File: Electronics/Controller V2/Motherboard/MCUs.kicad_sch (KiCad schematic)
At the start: 18 parts, among them J5 Pulse_J0011D01BNL, J7 Pulse_J0011D01BNL

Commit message: Working on V2 controller PCB.
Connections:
- net CAN_RX: no longer U5.45 (GPIO23_CRX1)
- net CAN_TX: no longer U5.44 (GPIO22_CTX1)
- no-connect marks 47 -> 49
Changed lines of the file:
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@@
   (no_connect (at 174.625 52.07))
   (no_connect (at 63.5 95.25))
+  (no_connect (at 235.585 46.99))
   (no_connect (at 174.625 95.25))
   (no_connect (at 174.625 97.79))
@@
   (no_connect (at 174.625 92.71))
   (no_connect (at 235.585 82.55))
+  (no_connect (at 235.585 49.53))
   (no_connect (at 174.625 49.53))
   (no_connect (at 235.585 59.69))
@@
     (stroke (width 0) (type default))
   )
-  (wire (pts (xy 235.585 46.99) (xy 247.015 46.99))
-    (stroke (width 0) (type default))
-  )
   (wire (pts (xy 92.71 116.84) (xy 90.17 116.84))
     (stroke (width 0) (type default))
@@
     (stroke (width 0) (type default))
   )
-  (wire (pts (xy 235.585 49.53) (xy 247.015 49.53))
-    (stroke (width 0) (type default))
-  )
   (wire (pts (xy 59.055 92.71) (xy 63.5 92.71))
     (stroke (width 0) (type default))
@@
     (stroke (width 0) (type default))
   )
-  (label "CAN_RX" (at 130.81 46.99 0) (fields_autoplaced)
-    (effects (font (size 1.27 1.27)) (justify left bottom))
-  )
-  (label "CAN_TX" (at 130.81 49.53 0) (fields_autoplaced)
-    (effects (font (size 1.27 1.27)) (justify left bottom))
-  )
   (hierarchical_label "IMU_SCK" (shape output) (at 133.985 72.39 0) (fields_autoplaced)
     (effects (font (size 1.27 1.27)) (justify left))
@@
     (effects (font (size 1.27 1.27)) (justify right))
   )
-  (hierarchical_label "CAN_TX" (shape output) (at 247.015 49.53 0) (fields_autoplaced)
+  (hierarchical_label "CAN_TX" (shape output) (at 130.81 49.53 0) (fields_autoplaced)
     (effects (font (size 1.27 1.27)) (justify left))
   )
@@
     (effects (font (size 1.27 1.27)) (justify left))
   )
-  (hierarchical_label "CAN_RX" (shape input) (at 247.015 46.99 0) (fields_autoplaced)
-    (effects (font (size 1.27 1.27)) (justify left))
-  )
+  (hierarchical_label "CAN_RX" (shape input) (at 130.81 46.99 0) (fields_autoplaced)
+    (effects (font (size 1.27 1.27)) (justify left))
+  )

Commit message: Added missing ground connection. Working on PCB layout.
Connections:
- net GPIO_G1: now also U4.38 (GPIO16_RX4_SCL1); no longer U4.41 (GPIO19_SCL0)
- net GPIO_G2: now also U4.39 (GPIO17_TX4_SDA1); no longer U4.40 (GPIO18_SDA0)
- net GPIO_G3: now also U4.40 (GPIO18_SDA0); no longer U4.39 (GPIO17_TX4_SDA1)
- net GPIO_G4: now also U4.41 (GPIO19_SCL0); no longer U4.38 (GPIO16_RX4_SCL1)
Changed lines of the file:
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@@
   (title_block
     (title "Tandem Leveller Controller")
-    (date "2026-02-02")
+    (date "2026-02-06")
     (rev "V2.0")
     (company "(C) andy@britishideas.com 2026")
@@
     (effects (font (size 1.27 1.27)) (justify right))
   )
-  (hierarchical_label "GPIO_G2" (shape bidirectional) (at 133.985 59.69 0) (fields_autoplaced)
+  (hierarchical_label "GPIO_G2" (shape bidirectional) (at 133.985 62.23 0) (fields_autoplaced)
     (effects (font (size 1.27 1.27)) (justify left))
   )
@@
     (effects (font (size 1.27 1.27)) (justify left))
   )
-  (hierarchical_label "GPIO_G4" (shape bidirectional) (at 133.985 64.77 0) (fields_autoplaced)
+  (hierarchical_label "GPIO_G4" (shape bidirectional) (at 133.985 57.15 0) (fields_autoplaced)
     (effects (font (size 1.27 1.27)) (justify left))
   )
@@
     (effects (font (size 1.27 1.27)) (justify right))
   )
-  (hierarchical_label "GPIO_G3" (shape bidirectional) (at 133.985 62.23 0) (fields_autoplaced)
+  (hierarchical_label "GPIO_G3" (shape bidirectional) (at 133.985 59.69 0) (fields_autoplaced)
     (effects (font (size 1.27 1.27)) (justify left))
   )
@@
     (effects (font (size 1.27 1.27)) (justify left))
   )
-  (hierarchical_label "GPIO_G1" (shape bidirectional) (at 133.985 57.15 0) (fields_autoplaced)
-    (effects (font (size 1.27 1.27)) (justify left))
-  )
+  (hierarchical_label "GPIO_G1" (shape bidirectional) (at 133.985 64.77 0) (fields_autoplaced)
+    (effects (font (size 1.27 1.27)) (justify left))
+  )

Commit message: Added generic IMU option.
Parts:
- added J10: ORIENT, Connector_PinHeader_2.54mm:PinHeader_1x02_P2.54mm_Vertical, symbol Connector_Generic:Conn_01x02
- added J11: OPT, Connector_PinHeader_2.54mm:PinHeader_1x02_P2.54mm_Vertical, symbol Connector_Generic:Conn_01x02
- added R22, R23: 10k, Resistor_SMD:R_0805_2012Metric, symbol Device:R
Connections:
- net +5V: now also R22.2, R23.2
- net GND: now also J10.1 (Pin_1), J11.1 (Pin_1)
- net at U4.18 (GPIO26_MOSI1): now also J10.2 (Pin_2), R22.1
- net at U4.19 (GPIO27_SCK1): now also J11.2 (Pin_2), R23.1
- net GPIO_G1 renamed GPIO_G1_RX
- net GPIO_G2 renamed GPIO_G2_TX
- no-connect marks 49 -> 47
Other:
- moved on the sheet: R1, R2

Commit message: Added relay to control output of valve E.
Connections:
- net VALVE_E_EN: now reaches U4.25 (GPIO33)
- no-connect marks 47 -> 46
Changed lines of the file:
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@@
   (title_block
     (title "Tandem Leveller Controller")
-    (date "2026-02-09")
+    (date "2026-03-01")
     (rev "V2.0")
     (company "(C) andy@britishideas.com 2026")
@@
   (no_connect (at 235.585 85.09))
   (no_connect (at 63.5 100.33))
-  (no_connect (at 124.46 95.25))
   (no_connect (at 63.5 97.79))
   (no_connect (at 235.585 90.17))
@@
     (stroke (width 0) (type default))
   )
+  (wire (pts (xy 124.46 95.25) (xy 133.985 95.25))
+    (stroke (width 0) (type default))
+  )
   (wire (pts (xy 34.925 127) (xy 34.925 139.7))
     (stroke (width 0) (type default))
@@
     (effects (font (size 1.27 1.27)) (justify right))
   )
+  (hierarchical_label "VALVE_E_EN" (shape output) (at 133.985 95.25 0) (fields_autoplaced)
+    (effects (font (size 1.27 1.27)) (justify left))
+  )
   (hierarchical_label "VALVE_E_PWM" (shape output) (at 57.785 67.31 180) (fields_autoplaced)

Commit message: Working on autosteer support for V2 controller.
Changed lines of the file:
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@@
   (title_block
     (title "Tandem Leveller Controller")
-    (date "2026-03-01")
+    (date "2026-03-02")
     (rev "V2.0")
     (company "(C) andy@britishideas.com 2026")
@@
     (effects (font (size 1.27 1.27)) (justify right))
   )
+  (hierarchical_label "WAS_SCL" (shape bidirectional) (at 114.935 168.91 0) (fields_autoplaced)
+    (effects (font (size 1.27 1.27)) (justify left))
+  )
+  (hierarchical_label "WAS_SDA" (shape bidirectional) (at 114.935 166.37 0) (fields_autoplaced)
+    (effects (font (size 1.27 1.27)) (justify left))
+  )
   (symbol (lib_id "power:+5V") (at 93.98 38.1 0) (unit 1)

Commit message: Added WAS circuit.
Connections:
- net GPIO_G3: now also U4.23 (GPIO31_CTX3); no longer U4.40 (GPIO18_SDA0)
- net GPIO_G4: now also U4.24 (GPIO32); no longer U4.41 (GPIO19_SCL0)
- net WAS_SCL: now also U4.41 (GPIO19_SCL0)
- net WAS_SDA: now also U4.40 (GPIO18_SDA0)
- net GPIO_C4: no longer names the net of U4.28 (GPIO36_CS)
- no-connect marks 46 -> 45
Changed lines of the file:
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@@
   (no_connect (at 174.625 59.69))
   (no_connect (at 235.585 95.25))
+  (no_connect (at 124.46 87.63))
   (no_connect (at 63.5 77.47))
   (no_connect (at 235.585 85.09))
-  (no_connect (at 63.5 100.33))
-  (no_connect (at 63.5 97.79))
   (no_connect (at 235.585 90.17))
   (no_connect (at 174.625 72.39))
@@
     (stroke (width 0) (type default))
   )
+  (wire (pts (xy 63.5 97.79) (xy 61.595 97.79))
+    (stroke (width 0) (type default))
+  )
   (wire (pts (xy 205.105 38.1) (xy 205.105 39.37))
     (stroke (width 0) (type default))
@@
     (stroke (width 0) (type default))
   )
+  (wire (pts (xy 61.595 121.285) (xy 66.675 121.285))
+    (stroke (width 0) (type default))
+  )
   (wire (pts (xy 124.46 74.93) (xy 133.985 74.93))
     (stroke (width 0) (type default))
@@
     (stroke (width 0) (type default))
   )
+  (wire (pts (xy 63.5 118.745) (xy 66.675 118.745))
+    (stroke (width 0) (type default))
+  )
   (wire (pts (xy 124.46 95.25) (xy 133.985 95.25))
     (stroke (width 0) (type default))
@@
     (stroke (width 0) (type default))
   )
+  (wire (pts (xy 61.595 97.79) (xy 61.595 121.285))
+    (stroke (width 0) (type default))
+  )
   (wire (pts (xy 271.145 113.665) (xy 271.145 104.775))
     (stroke (width 0) (type default))
@@
     (stroke (width 0) (type default))
   )
-  (wire (pts (xy 124.46 87.63) (xy 133.985 87.63))
-    (stroke (width 0) (type default))
-  )
   (wire (pts (xy 154.94 54.61) (xy 154.94 44.45))
     (stroke (width 0) (type default))
@@
     (stroke (width 0) (type default))
   )
+  (wire (pts (xy 63.5 100.33) (xy 63.5 118.745))
+    (stroke (width 0) (type default))
+  )
   (wire (pts (xy 201.295 116.84) (xy 201.295 118.11))
     (stroke (width 0) (type default))
@@
     (effects (font (size 1.27 1.27)) (justify left))
   )
-  (hierarchical_label "GPIO_G4" (shape bidirectional) (at 133.985 57.15 0) (fields_autoplaced)
-    (effects (font (size 1.27 1.27)) (justify left))
-  )
-  (hierarchical_label "GPIO_C4" (shape bidirectional) (at 133.985 87.63 0) (fields_autoplaced)
+  (hierarchical_label "GPIO_G4" (shape bidirectional) (at 66.675 118.745 0) (fields_autoplaced)
     (effects (font (size 1.27 1.27)) (justify left))
   )
@@
     (effects (font (size 1.27 1.27)) (justify right))
   )
-  (hierarchical_label "GPIO_G3" (shape bidirectional) (at 133.985 59.69 0) (fields_autoplaced)
+  (hierarchical_label "GPIO_G3" (shape bidirectional) (at 66.675 121.285 0) (fields_autoplaced)
     (effects (font (size 1.27 1.27)) (justify left))
   )
@@
     (effects (font (size 1.27 1.27)) (justify right))
   )
-  (hierarchical_label "WAS_SCL" (shape bidirectional) (at 114.935 168.91 0) (fields_autoplaced)
-    (effects (font (size 1.27 1.27)) (justify left))
-  )
-  (hierarchical_label "WAS_SDA" (shape bidirectional) (at 114.935 166.37 0) (fields_autoplaced)
-    (effects (font (size 1.27 1.27)) (justify left))
-  )
+  (hierarchical_label "WAS_SCL" (shape bidirectional) (at 133.985 57.15 0) (fields_autoplaced)
+    (effects (font (size 1.27 1.27)) (justify left))
+  )
+  (hierarchical_label "WAS_SDA" (shape bidirectional) (at 133.985 59.69 0) (fields_autoplaced)
+    (effects (font (size 1.27 1.27)) (justify left))
+  )

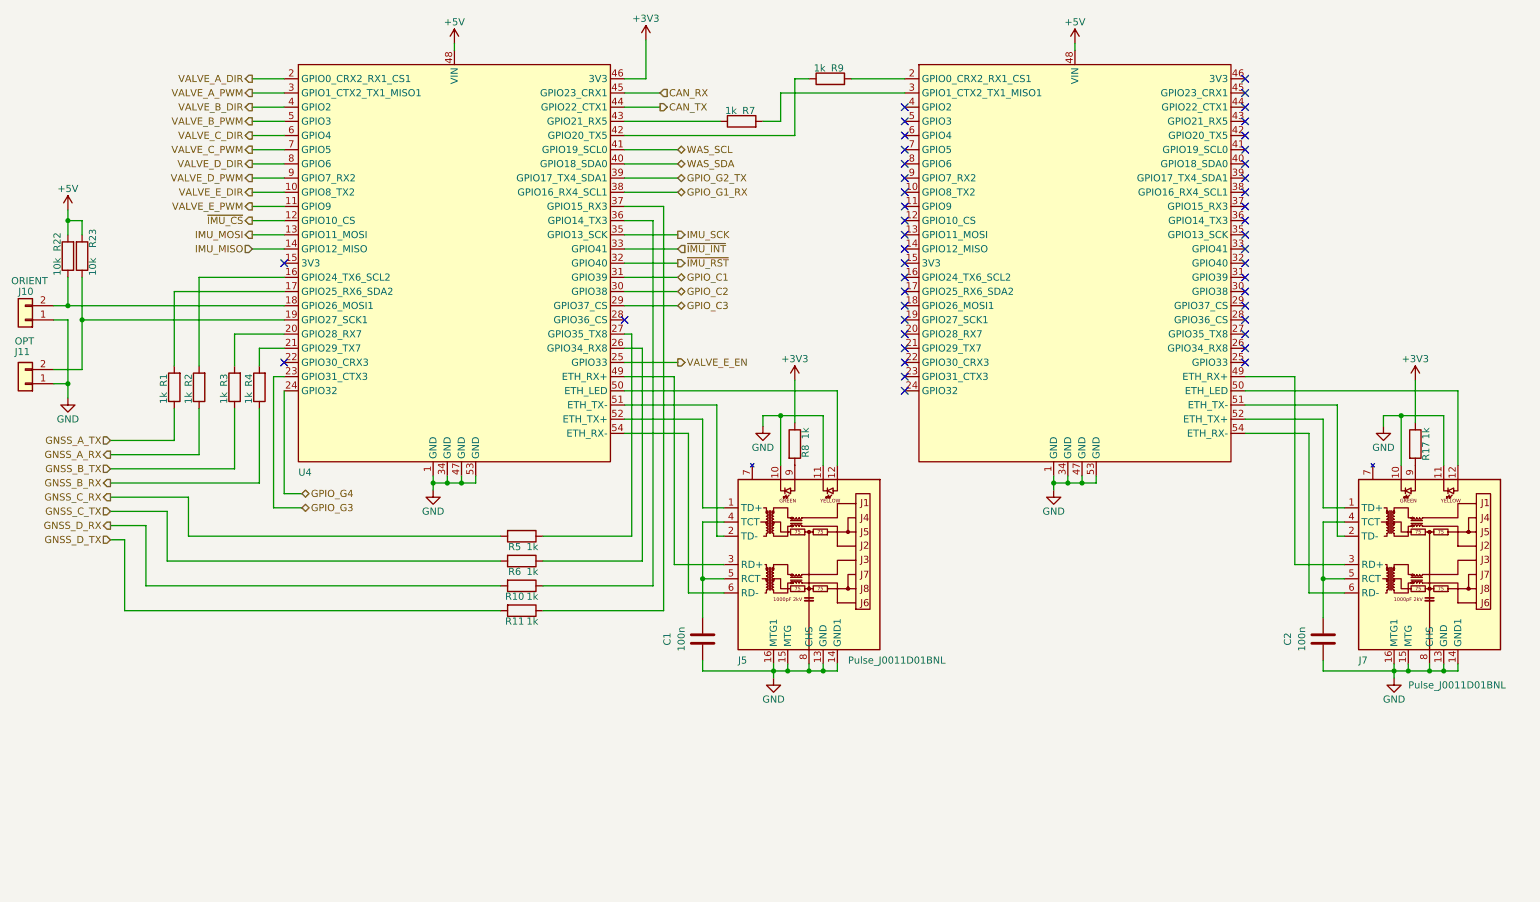
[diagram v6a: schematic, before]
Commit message: Added connector and mounting holes for future USB-C PD expansion board.
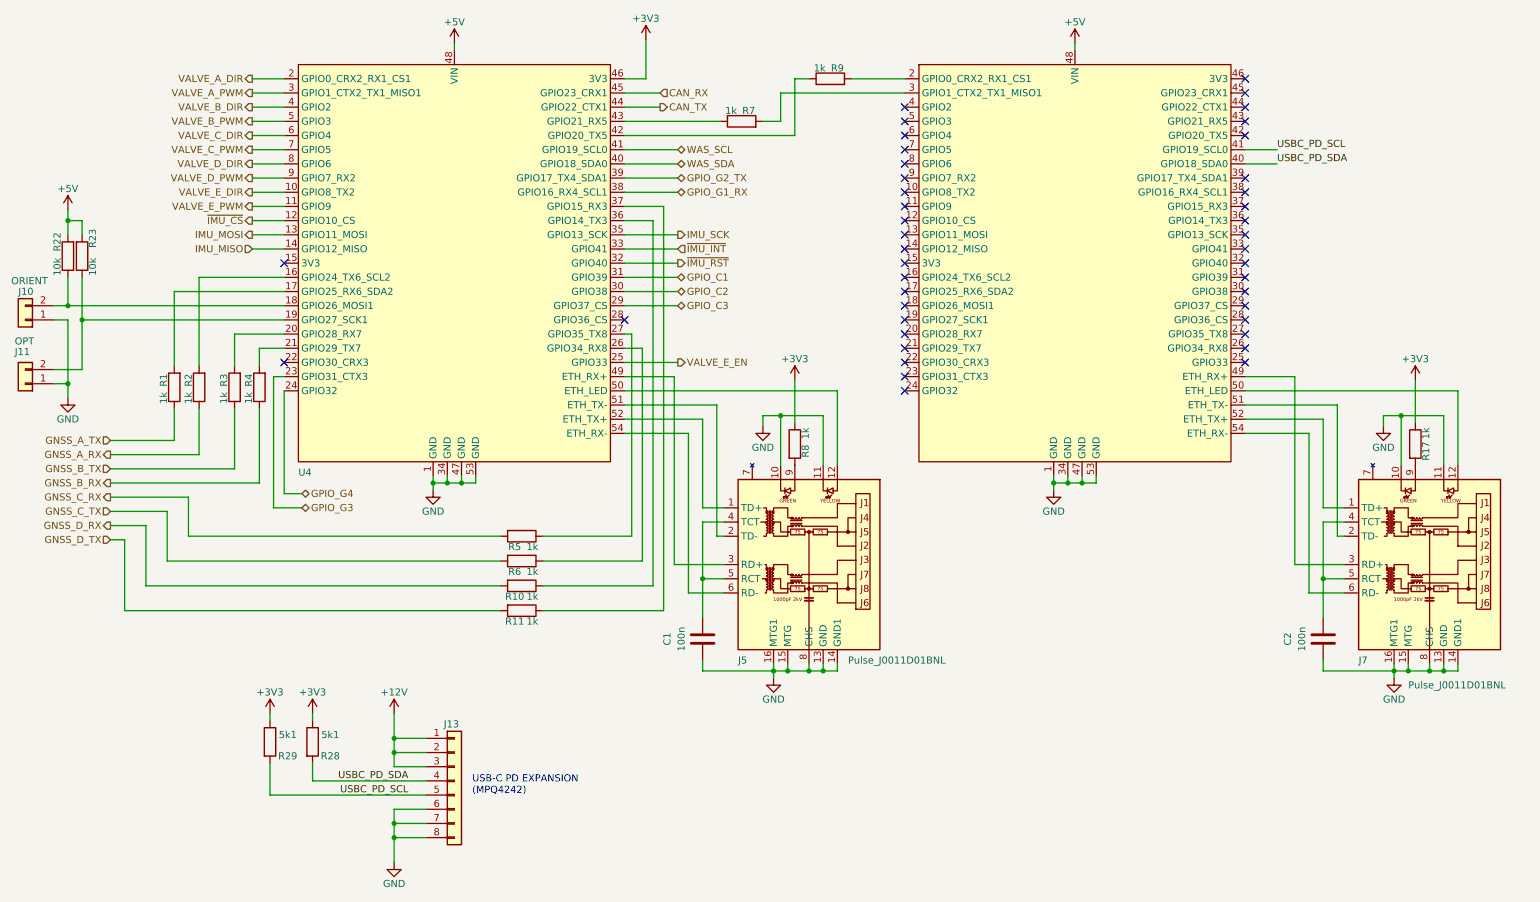
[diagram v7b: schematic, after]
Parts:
- added J13: Conn_01x10, Connector_JST:JST_XH_B8B-XH-A_1x08_P2.50mm_Vertical, symbol Connector_Generic:Conn_01x08
- added R28, R29: 5k1, Resistor_SMD:R_0805_2012Metric, symbol Device:R
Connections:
- net +3V3: now also R28.1, R29.1
- net GND: now also J13.6 (Pin_6), J13.7 (Pin_7), J13.8 (Pin_8)
- net USBC_PD_SDA: now reaches U5.40 (GPIO18_SDA0)
- net USBC_PD_SDA: now also J13.4 (Pin_4), R28.2
- net USBC_PD_SCL: now reaches U5.41 (GPIO19_SCL0)
- net USBC_PD_SCL: now also J13.5 (Pin_5), R29.2
- new net +12V: J13.1 (Pin_1), J13.2 (Pin_2), J13.3 (Pin_3)
- no-connect marks 45 -> 43
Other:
- note added: "USB-C PD EXPANSION (MPQ4242)"
